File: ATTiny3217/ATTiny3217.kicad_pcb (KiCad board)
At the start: 2 copper layers, 18 x 40.1 mm, 31 parts, among them J1 Conn_01x12, J3 Conn_01x12, U1 AP2204K-ADJ, U2 ATtiny3217-M

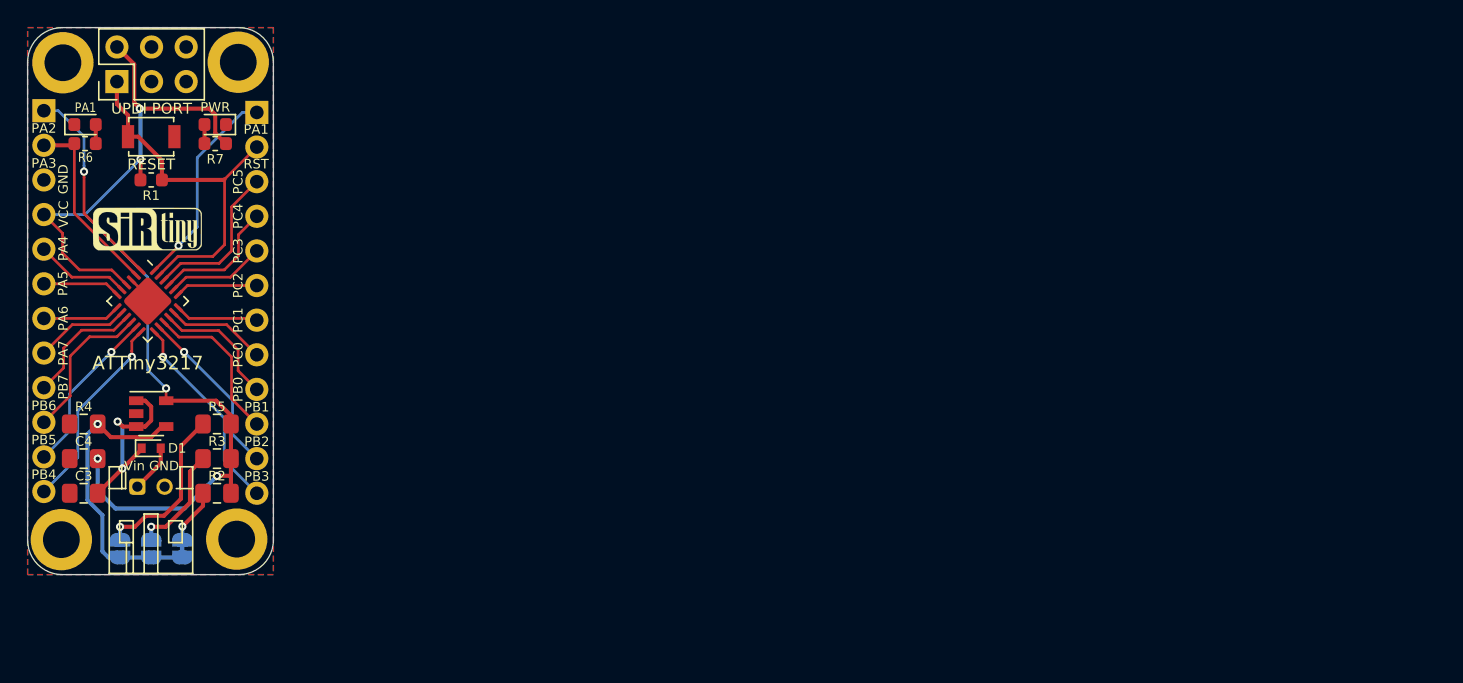
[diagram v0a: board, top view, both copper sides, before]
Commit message: Silkscreens Updated and Board Outlines aligned
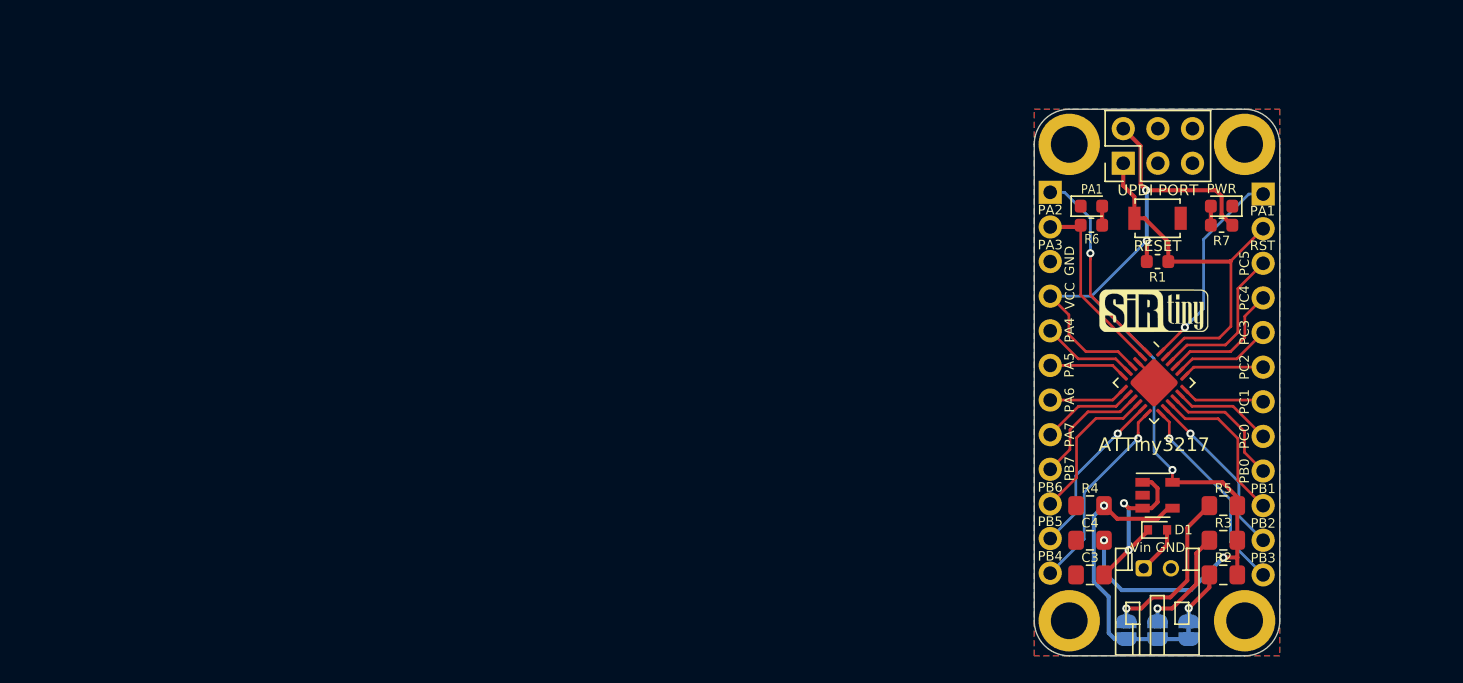
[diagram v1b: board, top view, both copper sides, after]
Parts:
- moved 1V8 74.1 mm to (153.1, 123.2)
- moved C3 74.1 mm to (150.4, 119.1)
- moved C4 74.1 mm to (150.4, 116.6)
- moved G*** 74.1 mm to (155.2, 95.3)
- moved G*** 74.1 mm to (155.1, 99.8)
- moved G*** 74.1 mm to (152.3, 101.0)
- moved PA1 74.1 mm to (150.5, 92.1)
- moved R2 74.1 mm to (160.2, 119.1)
- moved R3 74.1 mm to (160.2, 116.6)
- moved R4 74.1 mm to (150.4, 114.1)
- moved R5 74.1 mm to (160.2, 114.1)
- moved R6 74.1 mm to (150.5, 93.5)
- moved REF** 74.1 mm to (161.6, 122.5)
- moved REF** 74.1 mm to (148.9, 87.6)
- moved UPDI PORT 74.1 mm to (152.9, 88.9)
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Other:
- outline, holes or cut-outs redrawn

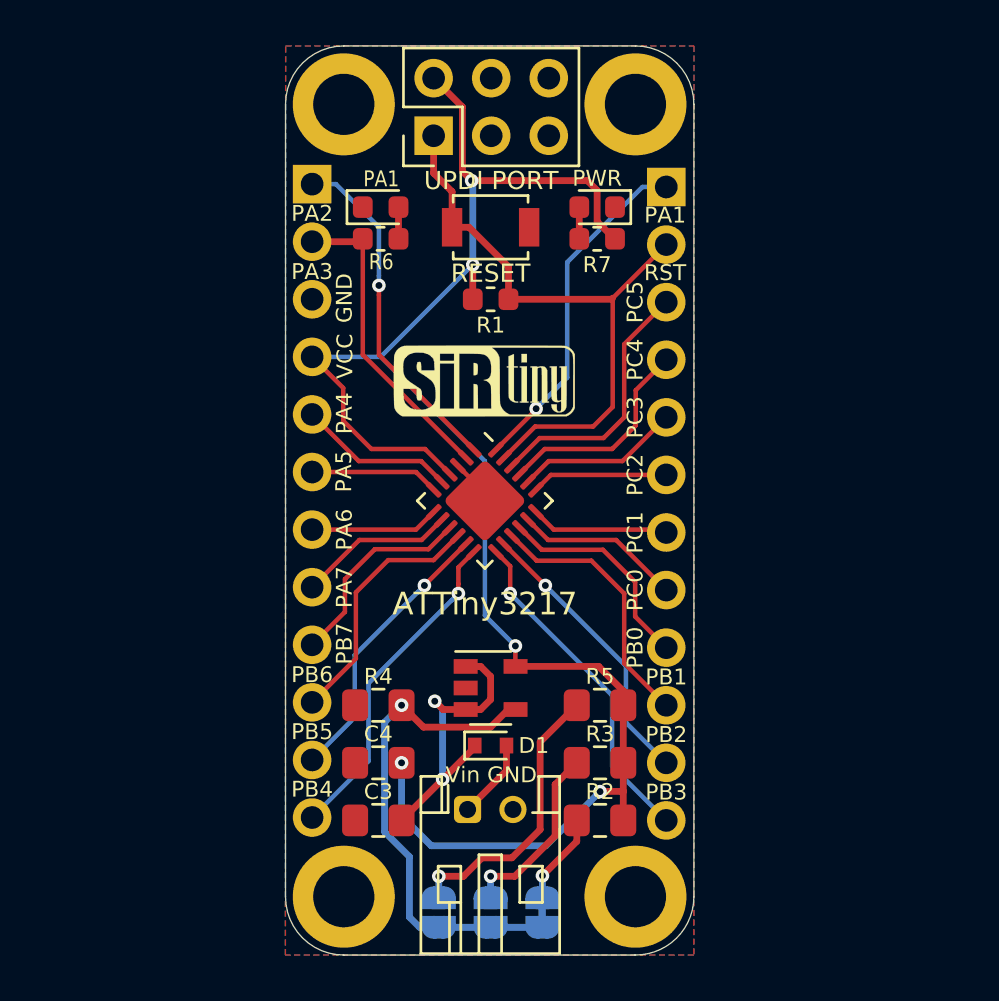
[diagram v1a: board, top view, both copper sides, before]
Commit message: Spacings Updated
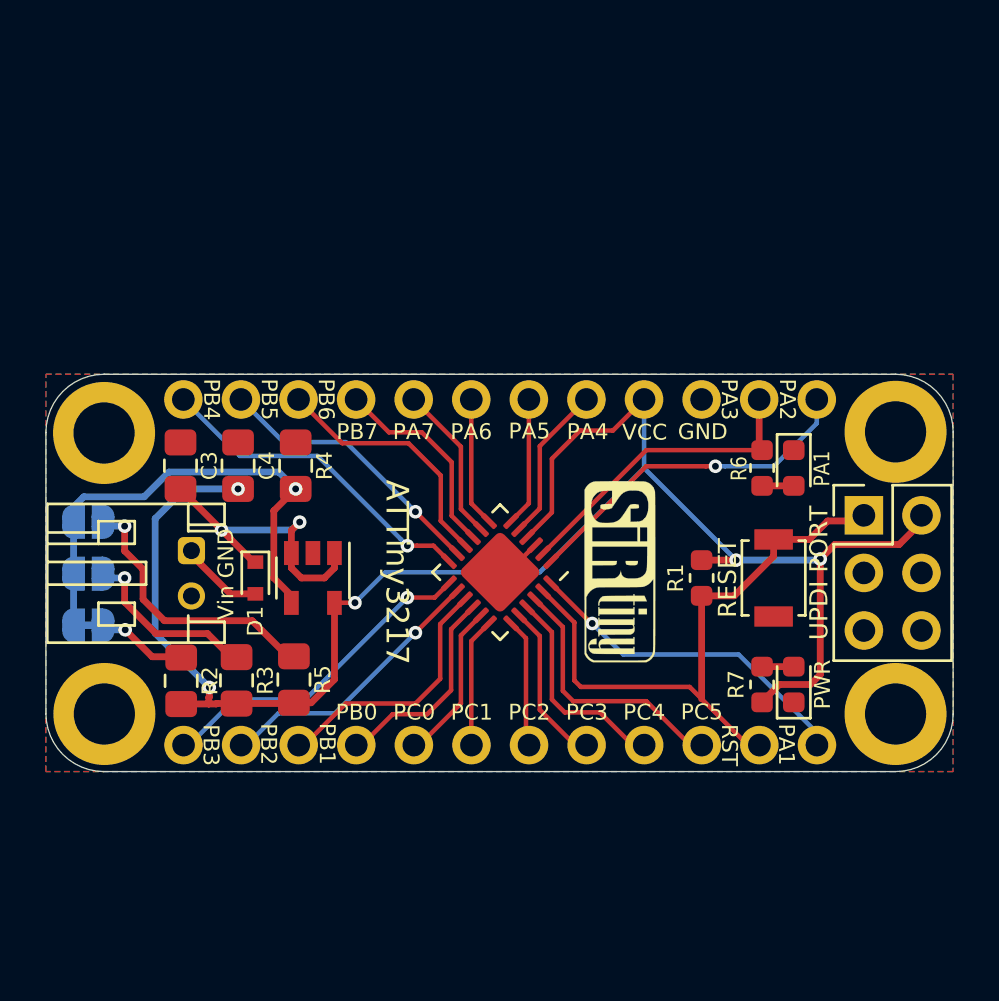
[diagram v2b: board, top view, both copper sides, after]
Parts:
- J1, J3: moved to F.Cu
- moved REF** 29.3 mm to (173.3, 114.5), turned to 270 degrees
- moved REF** 28.3 mm to (173.2, 102.0), turned to 270 degrees
- moved J3 25.5 mm to (169.8, 115.8), turned to 270 degrees
- moved UPDI PORT 25.3 mm to (171.8, 105.7), turned to 0 degrees
- moved REF** 24.7 mm to (138.3, 114.3), turned to 270 degrees
- moved J1 24.2 mm to (169.8, 100.6), turned to 270 degrees
- moved 5V 23.7 mm to (137.6, 110.5), turned to 180 degrees
- moved 3V3 23.2 mm to (137.6, 108.3), turned to 0 degrees
- moved 1V8 23.2 mm to (137.6, 106.0), turned to 0 degrees
- moved REF** 23.1 mm to (138.3, 101.9), turned to 270 degrees
- moved PWR 22.8 mm to (168.7, 113.2), turned to 90 degrees
- moved PA1 21.6 mm to (168.7, 103.6), turned to 270 degrees
- moved R7 21.0 mm to (167.3, 113.2), turned to 90 degrees
- moved RESET 19.9 mm to (167.8, 108.5), turned to 270 degrees
- moved R6 19.6 mm to (167.3, 103.6), turned to 270 degrees
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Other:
- board size 18 x 40.1 mm -> 40 x 17.5 mm

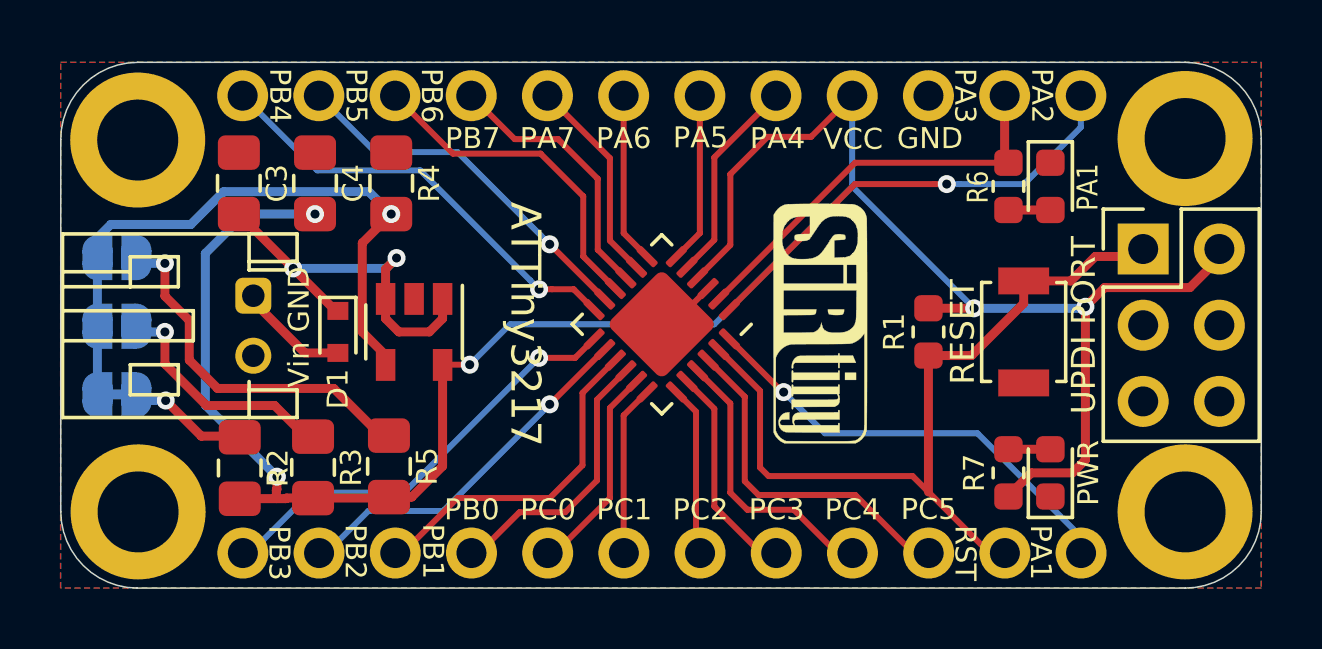
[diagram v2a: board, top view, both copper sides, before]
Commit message: Silkscreens Orientated
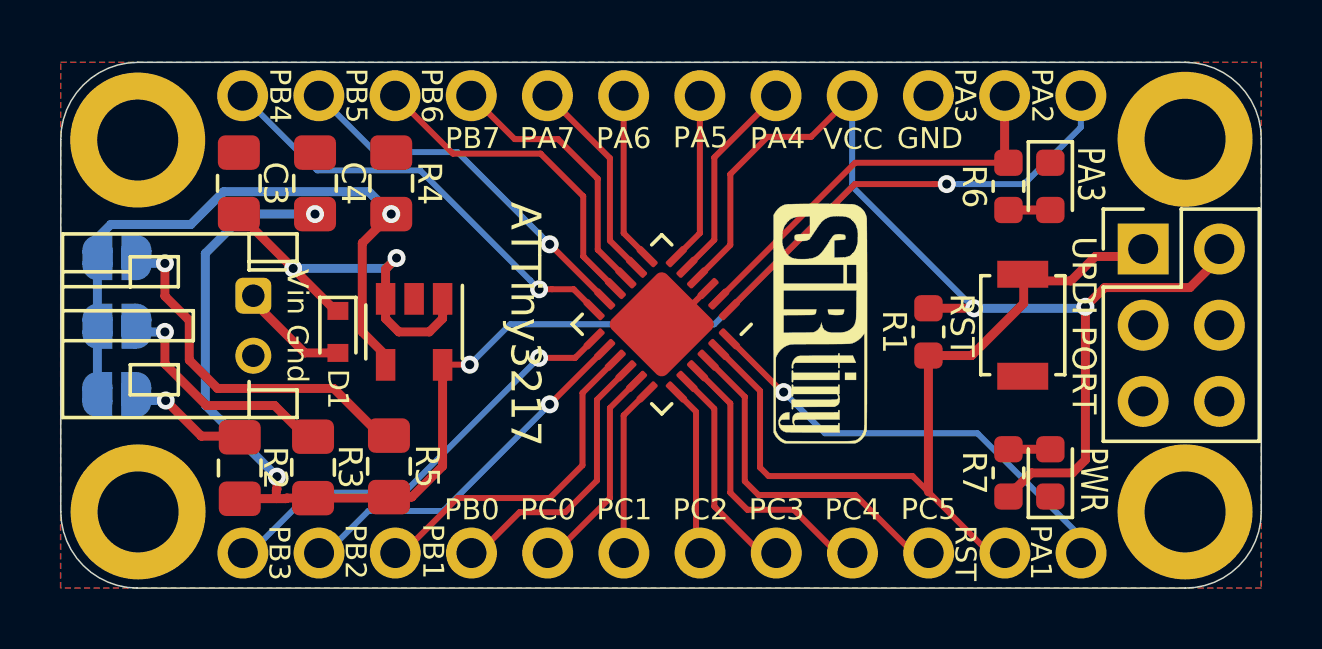
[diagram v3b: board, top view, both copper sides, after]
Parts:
- removed the 5V at (137.6, 110.5)
- added 5V: SolderJumper_2_Open, Jumper:SolderJumper-2_P1.3mm_Open_RoundedPad1.0x1.5mm, B.Cu at (137.6, 110.5)
- J1, J3: moved to B.Cu
- Vin Gnd: renamed from Vin GND
- moved G*** 0.25 mm to (153.9, 108.2)
- moved RST 0.23 mm to (167.8, 108.2)
- turned J1 to 90 degrees
- turned J3 to 90 degrees
- renumbered PA1 to PA3, RESET to RST
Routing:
- net Net-(5V1-Pad2): track 4.04 -> 0.00 mm, vias 1 -> 0
- net Net-(5V1-Pad1): track 0.00 -> 4.04 mm, vias 0 -> 1
